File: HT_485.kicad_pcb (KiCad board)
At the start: 2 copper layers, 75 x 40 mm, 56 parts, among them J1 POWER, J2 485, U1 ISL3179EIBZ, U2 SHT31-DIS + SF2, U3 LM2576D2TR4-3.3G, U4 STM32L010F4P6

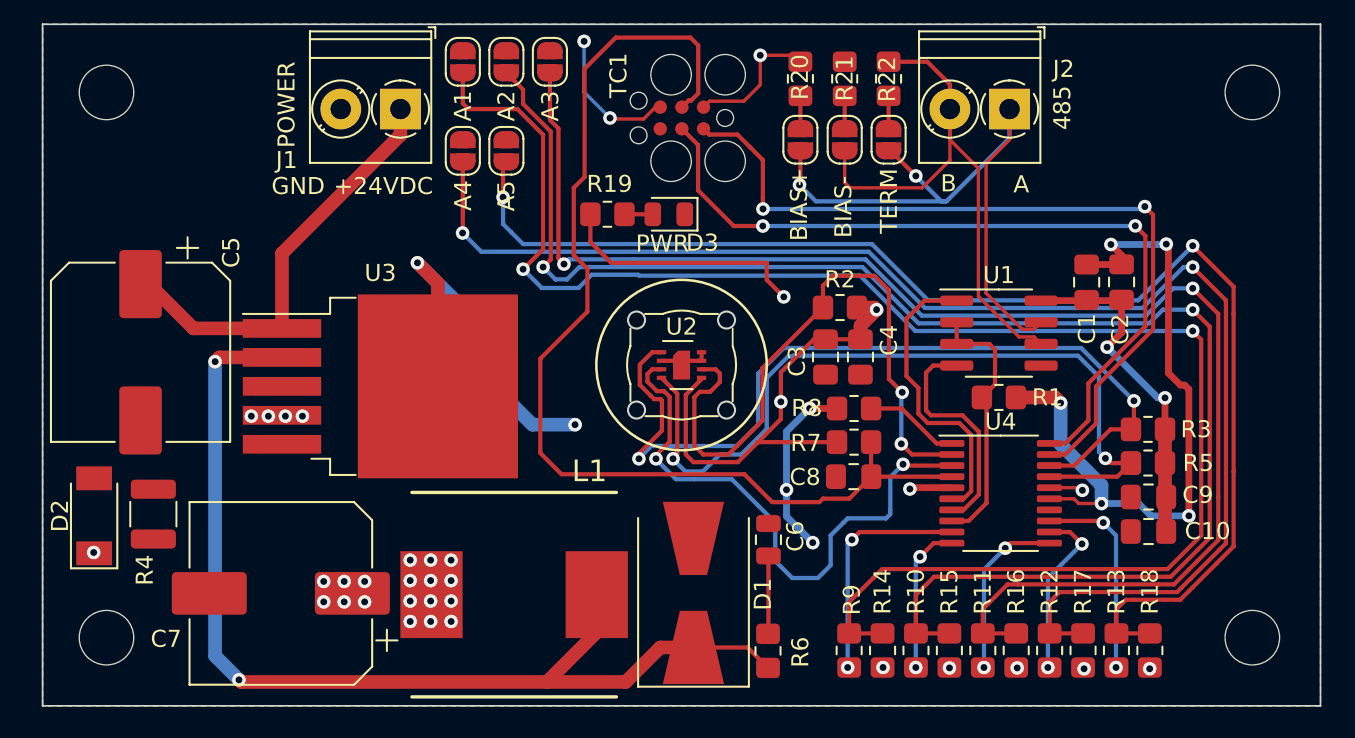
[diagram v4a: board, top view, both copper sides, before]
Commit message: Messa pompa di carica per 485 a 5V
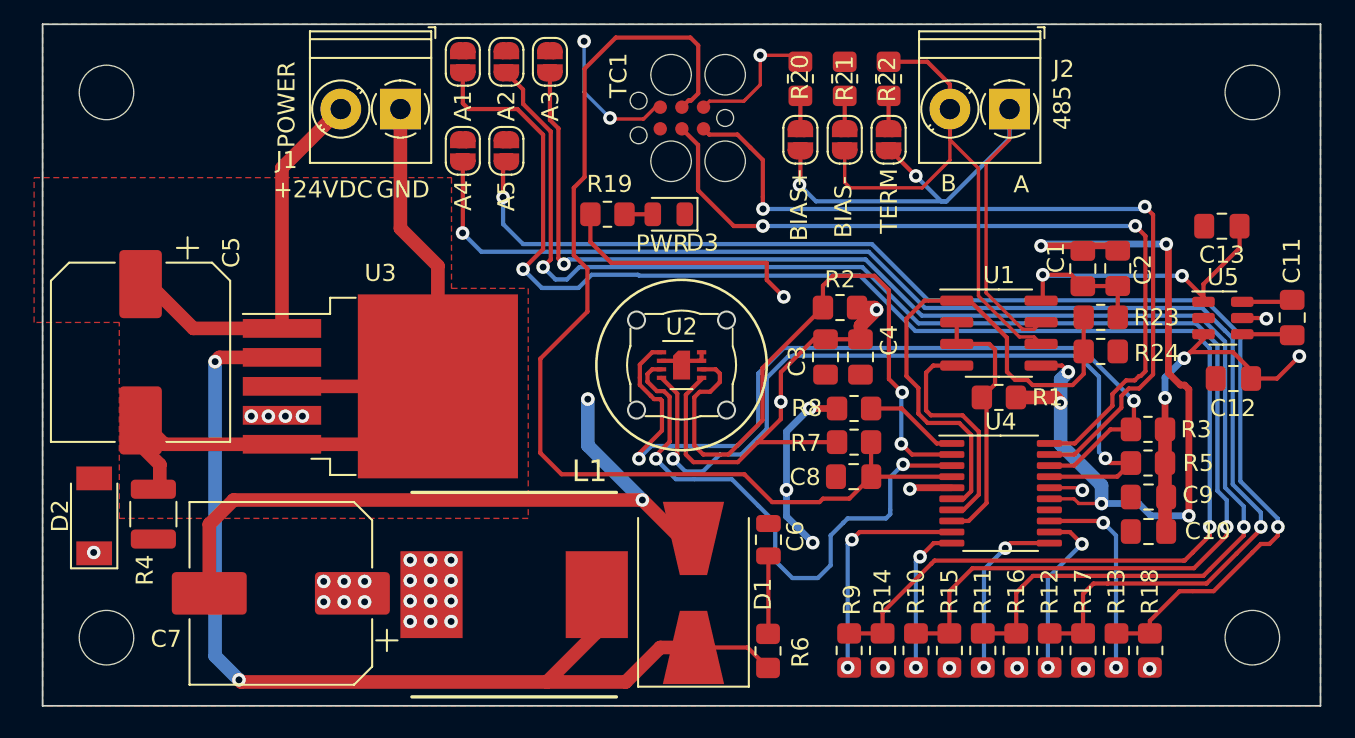
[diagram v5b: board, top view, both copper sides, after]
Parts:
- added C11: 1uF, Capacitor_SMD:C_0805_2012Metric_Pad1.18x1.45mm_HandSolder, F.Cu at (183.3, 83.2)
- added C12: 1uF, Capacitor_SMD:C_0805_2012Metric_Pad1.18x1.45mm_HandSolder, F.Cu at (179.9, 86.8)
- added C13: 1uF, Capacitor_SMD:C_0805_2012Metric_Pad1.18x1.45mm_HandSolder, F.Cu at (179.2, 77.8)
- added R23: 2K2, Resistor_SMD:R_0805_2012Metric_Pad1.20x1.40mm_HandSolder, F.Cu at (172.1, 83.2)
- added R24: 3K3, Resistor_SMD:R_0805_2012Metric_Pad1.20x1.40mm_HandSolder, F.Cu at (172.1, 85.2)
- added U5: CAT3200TDI-GT3, Package_TO_SOT_SMD:TSOT-23-6, F.Cu at (179.3, 83.2)
- D2: value 3.9V / 1W -> 5.1V / 1W
- U1: value ISL3179EIBZ -> MAX14786EAUD+T
- moved C1 0.83 mm to (171.1, 80.3)
- moved C2 0.83 mm to (173.1, 80.3)
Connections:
- C1 pad 2: +3V3 -> +5V
- C2 pad 2: +3V3 -> +5V
- C5 pad 2: GND -> Net-(C5-Pad2)
- J1 pad 1: +24V -> Net-(C5-Pad2)
- J1 pad 2: GND -> +24V
- R4 pad 2: GND -> Net-(C5-Pad2)
- U1 pad 8: +3V3 -> +5V
- U3 pad 3: GND -> Net-(C5-Pad2)
- U3 pad 5: GND -> Net-(C5-Pad2)
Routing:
- net Net-(C5-Pad2): track 0.00 -> 50.4 mm
- net GND: track 86.3 -> 115.0 mm, vias 12 -> 13
- net +5V: track 0.00 -> 23.7 mm, vias 0 -> 2
- net /RX: track 17.5 -> 31.8 mm
- net Net-(JP6-Pad1): track 78.0 -> 74.7 mm
- net Net-(C11-Pad1): track 0.00 -> 2.98 mm
- net Net-(C11-Pad2): track 0.00 -> 2.96 mm
- net Net-(JP8-Pad1): track 82.4 -> 80.1 mm
- net +3V3: track 75.8 -> 77.7 mm, vias 36 -> 38
- net Net-(JP4-Pad1): track 95.4 -> 93.8 mm
- net Net-(JP7-Pad1): track 89.7 -> 88.2 mm
- net Net-(JP5-Pad1): track 84.9 -> 83.4 mm
- net +24V: track 25.0 -> 23.5 mm
- net /SWCLK: track 46.4 -> 47.1 mm
- net /SWDIO: track 47.4 -> 48.1 mm
- added copper zone on F.Cu, net Net-(C5-Pad2)

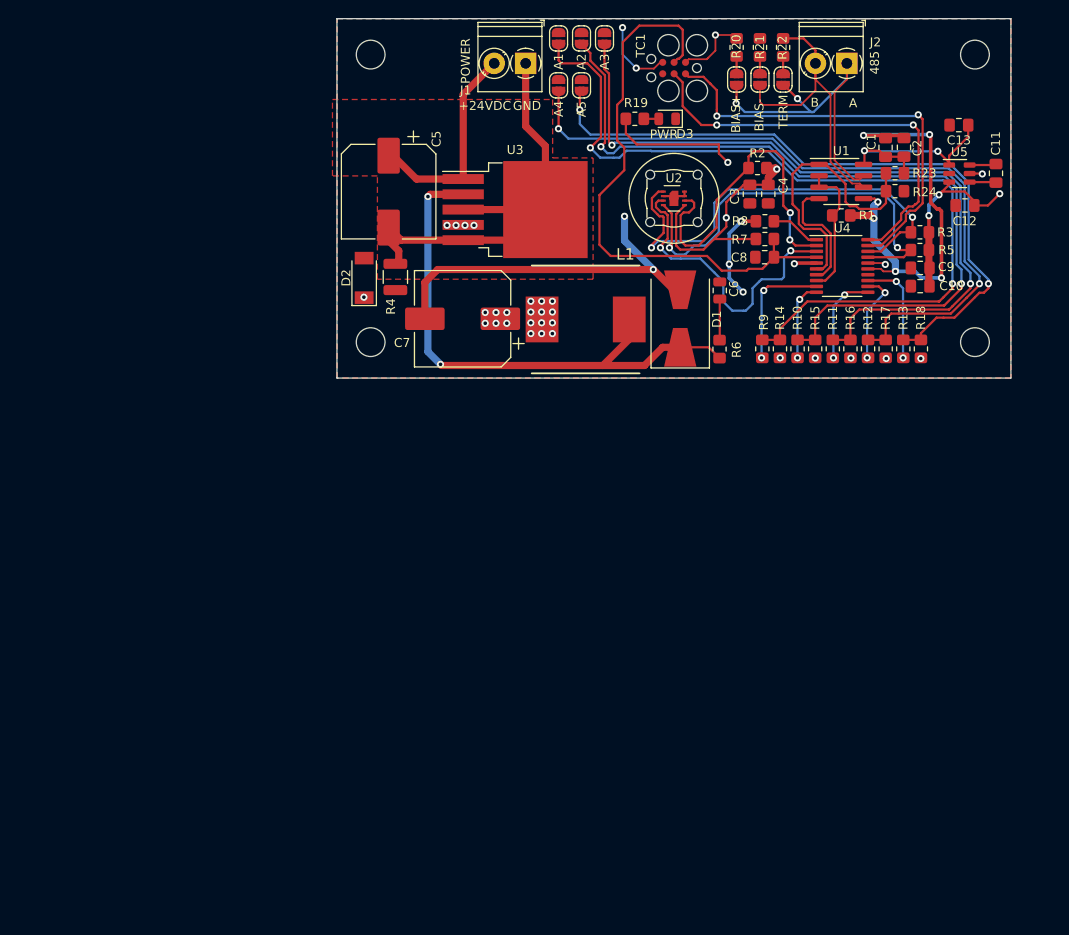
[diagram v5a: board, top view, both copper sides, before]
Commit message: Revisione 1.0.0.0 con PT1000
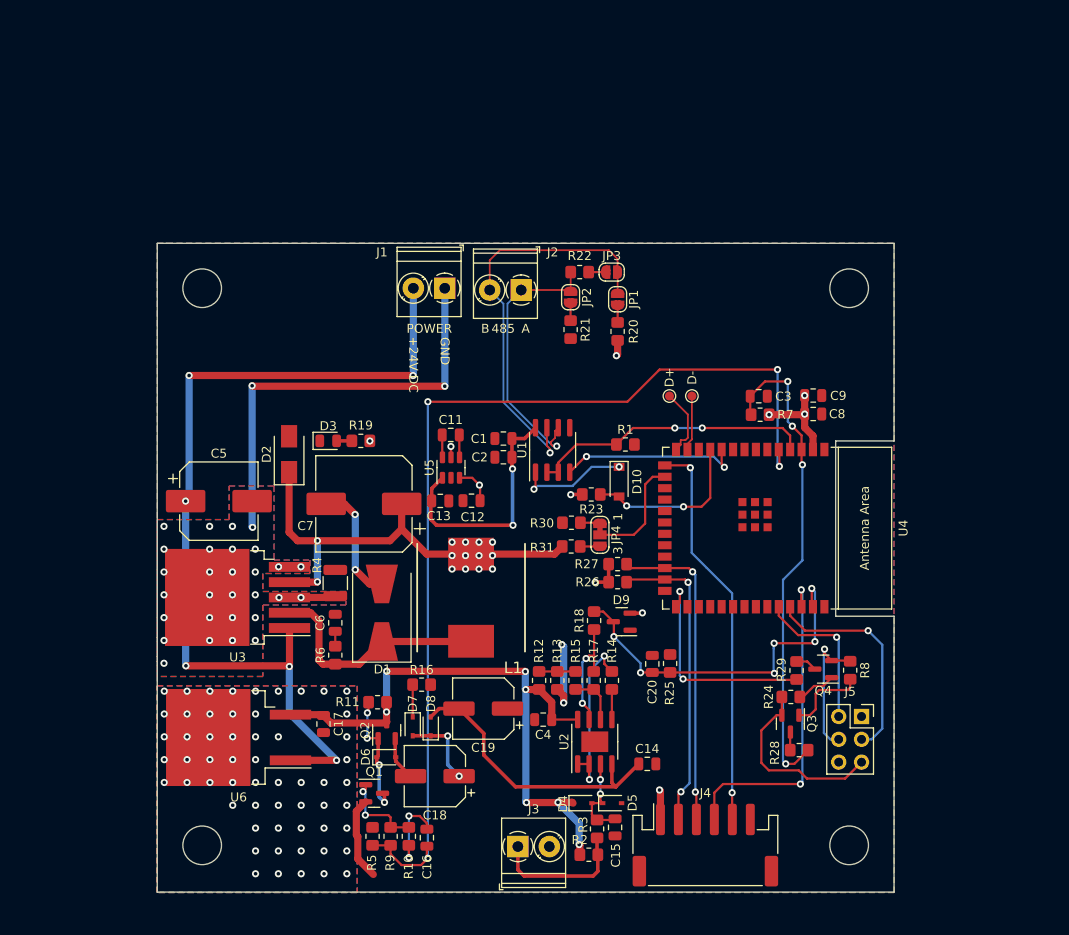
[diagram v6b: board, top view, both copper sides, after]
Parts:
- removed C10: 100nF, Capacitor_SMD:C_0805_2012Metric_Pad1.18x1.45mm_HandSolder
- removed JP5: A3, Jumper:SolderJumper-2_P1.3mm_Open_RoundedPad1.0x1.5mm
- removed JP6: A5, Jumper:SolderJumper-2_P1.3mm_Open_RoundedPad1.0x1.5mm
- removed JP7: A2, Jumper:SolderJumper-2_P1.3mm_Open_RoundedPad1.0x1.5mm
- removed JP8: A4, Jumper:SolderJumper-2_P1.3mm_Open_RoundedPad1.0x1.5mm
- removed the REF** at (113.8, 70.0)
- removed the REF** at (181.0, 102.0)
- removed the REF** at (113.8, 102.0)
- removed the REF** at (181.0, 70.0)
- removed SF2: SF2, HT485:SF2
- removed TC1: TC2030-IDC, TC2030:TC2030-IDC
- added C14: 100nF, Capacitor_SMD:C_0805_2012Metric, F.Cu at (144.5, 148.9)
- added C15: 100nF, Capacitor_SMD:C_0805_2012Metric, F.Cu at (141.0, 156.0)
- added C16: 1nF, Capacitor_SMD:C_0805_2012Metric, F.Cu at (120.0, 157.2)
- added C17: 1uF/25V, Capacitor_SMD:C_0805_2012Metric, F.Cu at (108.5, 144.5)
- added C18: 100uF/25V, Capacitor_SMD:CP_Elec_6.3x7.7, F.Cu at (120.9, 150.3)
- added C19: 100uF/25V, Capacitor_SMD:CP_Elec_6.3x7.7, F.Cu at (126.3, 142.8)
- added C20: 100nF, Capacitor_SMD:C_0805_2012Metric, F.Cu at (145.1, 137.8)
- added D10: STPS0520Z, Diode_SMD:D_SOD-123, F.Cu at (141.4, 117.5)
- added D4: 1N4148WS, Diode_SMD:D_SOD-323, F.Cu at (137.3, 153.3)
- added D5: 1N4148WS, Diode_SMD:D_SOD-323, F.Cu at (140.6, 153.3)
- added D6: 1N4148WS, Diode_SMD:D_SOD-323, F.Cu at (115.5, 148.2)
- added D7: 1N4148WS, Diode_SMD:D_SOD-323, F.Cu at (118.4, 144.8)
- added D8: 1N4148WS, Diode_SMD:D_SOD-323, F.Cu at (120.4, 144.8)
- added D9: BAV99, Package_TO_SOT_SMD:SOT-23, F.Cu at (141.7, 133.1)
- added J3: PT1000, TerminalBlock_Phoenix:TerminalBlock_Phoenix_PT-1,5-2-3.5-H_1x02_P3.50mm_Horizontal, F.Cu at (130.1, 158.1)
- added J4: H/T Sensor, Connector_JST:JST_PH_S6B-PH-SM4-TB_1x06-1MP_P2.00mm_Horizontal, F.Cu at (151.0, 158.0)
- added J5: PRG, Connector_PinSocket_2.54mm:PinSocket_2x03_P2.54mm_Vertical, F.Cu at (168.4, 143.7)
- added Q1: BC817, Package_TO_SOT_SMD:SOT-23, F.Cu at (114.1, 152.2)
- added Q2: BC817, Package_TO_SOT_SMD:SOT-23, F.Cu at (115.5, 145.2)
- added Q3: BC817, Package_TO_SOT_SMD:SOT-23, F.Cu at (160.5, 144.5)
- added Q4: BC817, Package_TO_SOT_SMD:SOT-23, F.Cu at (164.1, 138.4)
- added R25: 10K, Resistor_SMD:R_0805_2012Metric_Pad1.20x1.40mm_HandSolder, F.Cu at (147.1, 137.8)
- added R26: 10K, Resistor_SMD:R_0805_2012Metric_Pad1.20x1.40mm_HandSolder, F.Cu at (141.2, 128.7)
- added R27: 10K, Resistor_SMD:R_0805_2012Metric_Pad1.20x1.40mm_HandSolder, F.Cu at (141.2, 126.7)
- added R28: 0R, Resistor_SMD:R_0805_2012Metric_Pad1.20x1.40mm_HandSolder, F.Cu at (161.4, 147.4)
- added R29: 0R, Resistor_SMD:R_0805_2012Metric_Pad1.20x1.40mm_HandSolder, F.Cu at (161.1, 138.5)
- added R30: 10K, Resistor_SMD:R_0805_2012Metric_Pad1.20x1.40mm_HandSolder, F.Cu at (136.1, 122.1)
- added R31: 10K, Resistor_SMD:R_0805_2012Metric_Pad1.20x1.40mm_HandSolder, F.Cu at (136.1, 124.7)
- added REF**: MountingHole_4.3mm_M4, MountingHole:MountingHole_4.3mm_M4, F.Cu at (95.0, 96.0)
- added REF**: MountingHole_4.3mm_M4, MountingHole:MountingHole_4.3mm_M4, F.Cu at (167.0, 158.0)
- added REF**: MountingHole_4.3mm_M4, MountingHole:MountingHole_4.3mm_M4, F.Cu at (167.0, 96.0)
- added REF**: MountingHole_4.3mm_M4, MountingHole:MountingHole_4.3mm_M4, F.Cu at (95.0, 158.0)
- added TP1: D+, TestPoint:TestPoint_Pad_D1.0mm, F.Cu at (147.0, 108.0)
- added TP2: D-, TestPoint:TestPoint_Pad_D1.0mm, F.Cu at (149.5, 108.0)
- added U6: L7815, Package_TO_SOT_SMD:TO-263-2, F.Cu at (99.1, 146.0)
- C1, C11, C12, C13, C2, C8: footprint Capacitor_SMD:C_0805_2012Metric_Pad1.18x1.45mm_HandSolder -> Capacitor_SMD:C_0805_2012Metric
- C3: value 100nF -> 1uF/16V; footprint Capacitor_SMD:C_0805_2012Metric_Pad1.18x1.45mm_HandSolder -> Capacitor_SMD:C_0805_2012Metric
- C4: value 4.7uF -> 100nF; footprint Capacitor_SMD:C_0805_2012Metric_Pad1.18x1.45mm_HandSolder -> Capacitor_SMD:C_0805_2012Metric
- C5: value 100uF/75V -> 100uF / 50V; footprint Capacitor_SMD:CP_Elec_10x10 -> Capacitor_SMD:CP_Elec_8x10.5
- C9: value 4.7uF -> 10uF; footprint Capacitor_SMD:C_0805_2012Metric_Pad1.18x1.45mm_HandSolder -> Capacitor_SMD:C_0805_2012Metric
- D2: value 5.1V / 1W -> 3.9V/1W; footprint Diode_SMD:D_SOD-128 -> Diode_SMD:D_SMA
- JP4: value A1 -> UART_BOOT_MSG; footprint Jumper:SolderJumper-2_P1.3mm_Open_RoundedPad1.0x1.5mm -> Jumper:SolderJumper-3_P1.3mm_Bridged12_RoundedPad1.0x1.5mm_NumberLabels
- R10: value 1K -> 100R
- R11: value 1K -> 10K
- R15: value 10K -> 1K
- R16: value 10K -> 10R
- R17: value 10K -> 3k3
- R2: value 10K -> 1K 1%
- R23: value 2K2 -> 4K7
- R24: value 3K3 -> 10K
- R7, R8: value 4K7 -> 10K
- U2: value SHT31-DIS + SF2 -> TL082; footprint HT485:Sensirion_DFN-8-1EP_2.5x2.5mm_P0.5mm_EP1.1x1.7mm -> Package_SO:SOIC-8-1EP_3.9x4.9mm_P1.27mm_EP2.29x3mm
- U4: value STM32L010F4P6 -> ESP32-S3-WROOM-1-N16R8; footprint Package_SO:TSSOP-20_4.4x6.5mm_P0.65mm -> Espressif:ESP32-S3-WROOM-1
- moved R5 89.3 mm to (114.0, 157.0), turned to 90 degrees
- moved R2 78.7 mm to (138.0, 159.0)
- moved R3 75.5 mm to (138.9, 156.2), turned to -90 degrees
- moved C13 71.3 mm to (121.5, 119.7), turned to 0 degrees
- moved R10 69.4 mm to (118.0, 157.0)
- moved R9 68.2 mm to (116.0, 157.0)
- moved C11 67.3 mm to (122.7, 112.3), turned to 0 degrees
- moved U5 65.4 mm to (122.7, 116.0), turned to 90 degrees
- moved R11 64.1 mm to (114.5, 142.1), turned to 180 degrees
- moved C12 64.0 mm to (125.0, 119.6)
- moved C4 63.6 mm to (133.0, 144.0), turned to 180 degrees
- moved U2 61.1 mm to (138.7, 146.5), turned to 90 degrees
- moved R16 60.6 mm to (119.4, 140.1), turned to 0 degrees
- moved R24 57.5 mm to (160.5, 141.5), turned to 0 degrees
- moved C6 56.6 mm to (109.8, 133.2)
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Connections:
- C3 pad 1: GND -> /EN
- C3 pad 2: +3V3 -> GND
- C4 pad 1: GND -> +15V
- C4 pad 2: +3V3 -> GND
- C8 pad 1: /NRESET -> +3V3
- C9 pad 1: GND -> +3V3
- C9 pad 2: +3V3 -> GND
- J2 pad 1: /485+ -> /485-
- J2 pad 2: /485- -> /485+
- JP4 pad 2: GND -> Net-(JP4-Pad2)
- R10 pad 1: Net-(JP7-Pad1) -> Net-(Q1-Pad1)
- R10 pad 2: Net-(R10-Pad2) -> Net-(C16-Pad2)
- R11 pad 1: Net-(JP5-Pad1) -> +15V
- R11 pad 2: Net-(R11-Pad2) -> Net-(D6-Pad1)
- R12 pad 1: Net-(JP8-Pad1) -> +15V
- R13 pad 1: Net-(JP6-Pad1) -> Net-(R12-Pad2)
- R13 pad 2: Net-(R13-Pad2) -> GND
- R14 pad 1: +3V3 -> Net-(R14-Pad1)
- R14 pad 2: Net-(JP4-Pad1) -> Net-(R14-Pad2)
- R15 pad 1: +3V3 -> Net-(R12-Pad2)
- R15 pad 2: Net-(JP7-Pad1) -> Net-(R15-Pad2)
- R16 pad 1: +3V3 -> Net-(D7-Pad1)
- R16 pad 2: Net-(JP5-Pad1) -> GND
- R17 pad 1: +3V3 -> Net-(R15-Pad2)
- R17 pad 2: Net-(JP8-Pad1) -> Net-(R17-Pad2)
- R18 pad 1: +3V3 -> Net-(R17-Pad2)
- R18 pad 2: Net-(JP6-Pad1) -> /PT1000_ADC
- R2 pad 1: /RESET -> +15V
- R2 pad 2: +3V3 -> Net-(J3-Pad1)
- R23 pad 2: +5V -> +3V3
- R24 pad 1: GND -> /RTS
- R24 pad 2: /RX -> Net-(Q4-Pad1)
- R3 pad 1: /SDA -> Net-(C15-Pad1)
- R3 pad 2: +3V3 -> Net-(J3-Pad1)
- R5 pad 1: /SCL -> /OP_NEG_V_PWM
- R5 pad 2: +3V3 -> GND
- R7 pad 1: /NRESET -> /EN
- R8 pad 1: GND -> /DTR
- R8 pad 2: Net-(R8-Pad2) -> Net-(Q3-Pad1)
- R9 pad 1: Net-(JP4-Pad1) -> Net-(Q1-Pad1)
- R9 pad 2: Net-(R9-Pad2) -> /OP_NEG_V_PWM
- U1 pad 1: /RX -> Net-(D10-Pad1)
- U2 pad 1: /SDA -> Net-(R14-Pad2)
- U2 pad 2: GND -> Net-(R14-Pad2)
- U2 pad 3: /ALERT -> Net-(C15-Pad1)
- U2 pad 4: /SCL -> -12V
- U2 pad 5: +3V3 -> Net-(R14-Pad1)
- U2 pad 6: /RESET -> Net-(R15-Pad2)
- U2 pad 7: GND -> Net-(R17-Pad2)
- U2 pad 8: GND -> +15V
- U2 pad 9: GND -> (no net)
- U4 pad 1: Net-(R8-Pad2) -> GND
- U4 pad 10: Net-(R10-Pad2) -> /TX
- U4 pad 11: Net-(R11-Pad2) -> /RX
- U4 pad 12: Net-(R12-Pad2) -> unconnected-(U4-Pad12)
- U4 pad 13: Net-(R13-Pad2) -> /D-
- U4 pad 14: unconnected-(U4-Pad14) -> /D+
- U4 pad 15: GND -> /ALERT
- U4 pad 16: +3V3 -> Net-(JP4-Pad2)
- U4 pad 17: /SCL -> unconnected-(U4-Pad17)
- U4 pad 18: /SDA -> unconnected-(U4-Pad18)
- U4 pad 19: /SWDIO -> unconnected-(U4-Pad19)
- U4 pad 2: /RESET -> +3V3
- U4 pad 20: /SWCLK -> unconnected-(U4-Pad20)
- U4 pad 3: /ALERT -> /EN
- U4 pad 4: /NRESET -> /DE
- U4 pad 5: +3V3 -> /OP_NEG_V_PWM
- U4 pad 6: /RX -> unconnected-(U4-Pad6)
- U4 pad 7: /TX -> unconnected-(U4-Pad7)
- U4 pad 8: /DE -> unconnected-(U4-Pad8)
- U4 pad 9: Net-(R9-Pad2) -> unconnected-(U4-Pad9)
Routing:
- net /OP_NEG_V_PWM: track 0.00 -> 113.3 mm, vias 0 -> 4
- net Net-(JP4-Pad1): track 93.8 -> 2.19 mm, vias 2 -> 0
- net Net-(JP7-Pad1): track 88.2 -> 0.00 mm, vias 2 -> 0
- net GND: track 115.0 -> 31.1 mm, vias 13 -> 4
- net Net-(JP5-Pad1): track 83.4 -> 0.00 mm, vias 2 -> 0
- net Net-(JP8-Pad1): track 80.1 -> 0.00 mm, vias 2 -> 0
- net +24V: track 23.5 -> 100.7 mm, vias 0 -> 6
- net Net-(JP6-Pad1): track 74.7 -> 0.00 mm, vias 2 -> 0
- net +15V: track 0.00 -> 68.3 mm, vias 0 -> 7
- net /NRESET: track 64.0 -> 0.00 mm
- net /EN: track 0.00 -> 54.3 mm, vias 0 -> 4
- net /SWDIO: track 48.1 -> 0.00 mm, vias 2 -> 0
- net /SWCLK: track 47.1 -> 0.00 mm, vias 2 -> 0
- net /PT1000_ADC: track 0.00 -> 40.7 mm, vias 0 -> 6
- net Net-(D1-Pad1): track 62.1 -> 26.2 mm, vias 2 -> 0
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- added copper zone on B.Cu, net Net-(C17-Pad2)
- added copper zone on F.Cu, net Net-(C17-Pad2)
- added copper zone on B.Cu, net Net-(C5-Pad2)
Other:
- board size 75 x 40 mm -> 82 x 72.2 mm
- board text added: "${COMPANY} ${TITLE} V: ${REVISION} DATE: ${ISSUE_DATE} ${COMMENT1}"
- board text added: "+24V DC"
- board text removed: "+24VDC"
- board text removed: "BIAS+"
- board text removed: "BIAS-"
- board text removed: "TERM"

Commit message: Cambiata traccia per 3v3 e alimentatore switching
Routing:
- net +3V3: track 77.2 -> 72.7 mm
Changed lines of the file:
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@@
     (property "Sheetname" "")
     (attr smd)
-    (fp_text reference "U4" (at 0 -17.05 90) (layer "F.SilkS")
+    (fp_text reference "U4" (at -11.2712 -11.8842 90) (layer "F.SilkS")
       (effects (font (size 1 1) (thickness 0.15)))
     )
@@
   (segment (start 107.823 124.1044) (end 105.6212 124.1044) (width 0.8) (layer "F.Cu") (net 2))
   (segment (start 137.302002 118.952998) (end 136.037602 118.952998) (width 0.4) (layer "F.Cu") (net 2))
-  (segment (start 134.2198 125.5886) (end 124.925 125.5886) (width 0.8) (layer "F.Cu") (net 2))
   (segment (start 117.2 122.8) (end 117.2 120) (width 0.8) (layer "F.Cu") (net 2))
-  (segment (start 135.0678 124.7406) (end 134.2198 125.5886) (width 0.8) (layer "F.Cu") (net 2))
+  (segment (start 137.795 128.7272) (end 138.7348 128.7272) (width 0.8) (layer "F.Cu") (net 2))
   (segment (start 141.2324 101.81) (end 141.2324 103.3696) (width 0.8) (layer "F.Cu") (net 2))
   (segment (start 142.6265 132.1629) (end 143.9605 132.1629) (width 0.4) (layer "F.Cu") (net 2))
@@
   (segment (start 162.9744 113.951) (end 162.9744 112.4284) (width 0.8) (layer "F.Cu") (net 2))
   (segment (start 146 155.1222) (end 146 151.9436) (width 0.8) (layer "F.Cu") (net 2))
+  (segment (start 135.0678 126) (end 137.795 128.7272) (width 0.8) (layer "F.Cu") (net 2))
   (segment (start 162.05 111.504) (end 162.05 110.0094) (width 0.8) (layer "F.Cu") (net 2))
   (segment (start 125.9258 119.6436) (end 125.9258 117.9756) (width 0.25) (layer "F.Cu") (net 2))
@@
   (segment (start 125.9258 117.9756) (end 125.857 117.9068) (width 0.25) (layer "F.Cu") (net 2))
   (segment (start 107.823 124.1044) (end 115.8956 124.1044) (width 0.8) (layer "F.Cu") (net 2))
+  (segment (start 135.0678 124.7406) (end 135.0678 126) (width 0.8) (layer "F.Cu") (net 2))
   (via (at 162.05 110.0094) (size 0.8) (drill 0.4) (layers "F.Cu" "B.Cu") (net 2))
   (via (at 113.665 113.0046) (size 0.8) (drill 0.4) (layers "F.Cu" "B.Cu") (net 2))

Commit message: Remaster
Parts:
- removed R4: 0R / 0.5 W, Resistor_SMD:R_1210_3225Metric
- C13: value 1uF -> 10uF
- moved D2 62.5 mm to (166.5, 105.0), turned to 0 degrees
- moved R19 20.5 mm to (104.4, 94.2), turned to 0 degrees
- moved D3 18.7 mm to (109.0, 94.3)
- moved C6 10.8 mm to (119.5, 128.5)
- moved R6 10.6 mm to (119.5, 132.5)
- moved L1 2.08 mm to (127.0, 130.4)
- moved TP1 2.00 mm to (147.0, 110.0)
- moved TP2 2.00 mm to (149.5, 110.0)
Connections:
- C17 pad 2: Net-(C17-Pad2) -> GND
- C5 pad 2: Net-(C5-Pad2) -> GND
- J1 pad 1: Net-(C5-Pad2) -> GND
- U3 pad 3: Net-(C5-Pad2) -> GND
- U3 pad 5: Net-(C5-Pad2) -> GND
- U6 pad 2: Net-(C17-Pad2) -> GND
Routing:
- net GND: track 31.1 -> 145.7 mm, vias 4 -> 3
- net /OP_NEG_V_PWM: track 113.3 -> 0.00 mm, vias 4 -> 0
- net +15V: track 68.3 -> 0.00 mm, vias 7 -> 0
- net /EN: track 54.3 -> 0.00 mm, vias 4 -> 0
- net Net-(C5-Pad2): track 53.3 -> 0.00 mm, vias 31 -> 0
- net /485+: track 46.1 -> 0.00 mm, vias 1 -> 0
- net +3V3: track 72.7 -> 117.3 mm, vias 25 -> 6
- net /ALERT: track 44.0 -> 0.00 mm, vias 2 -> 0
- net /PT1000_ADC: track 40.7 -> 0.00 mm, vias 6 -> 0
- net /RESET: track 36.6 -> 0.00 mm, vias 2 -> 0
- net /SDA: track 35.4 -> 0.00 mm, vias 2 -> 0
- net /SCL: track 34.1 -> 0.00 mm, vias 2 -> 0
- net -12V: track 32.3 -> 0.00 mm
- net /DE: track 31.6 -> 0.00 mm, vias 2 -> 0
- net /485-: track 31.1 -> 0.00 mm, vias 1 -> 0
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- removed copper zone on B.Cu, net +3V3
- removed copper zone on B.Cu, net Net-(C17-Pad2)
- removed copper zone on F.Cu, net Net-(C17-Pad2)
- removed copper zone on B.Cu, net Net-(C5-Pad2)
- removed copper zone on F.Cu, net Net-(C5-Pad2)
